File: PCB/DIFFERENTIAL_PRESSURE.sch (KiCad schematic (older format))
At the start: 6 parts

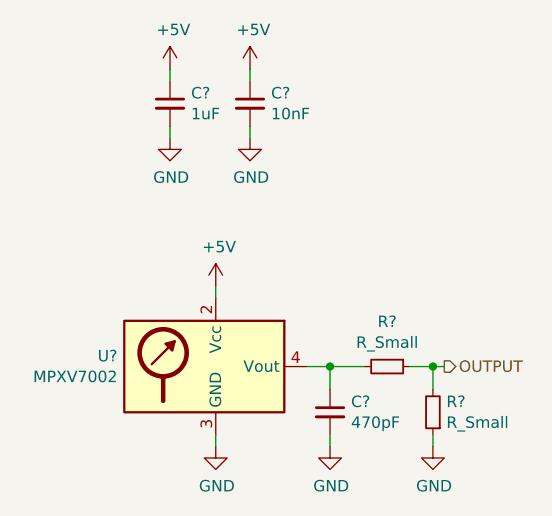
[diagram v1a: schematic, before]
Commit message: Connected Differential pressure sensor
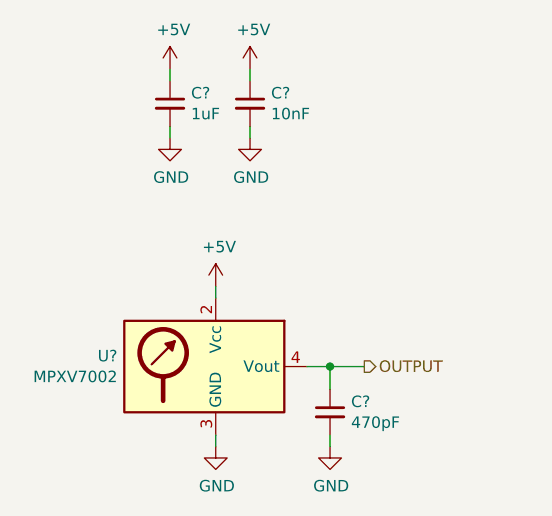
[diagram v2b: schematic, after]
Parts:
- removed R? (x2): R_Small, symbol Device:R_Small
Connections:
- net OUTPUT: now also C?.1, U?.4 (Vout)
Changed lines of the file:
@@
 Wire Wire Line
 	6550 4150 6550 4200
-$Comp
-L Device:R_Small R?
-U 1 1 5E8DE8A9
-P 6800 3850
-F 0 "R?" V 6604 3850 50  0000 C CNN
-F 1 "R_Small" V 6695 3850 50  0000 C CNN
-F 2 "" H 6800 3850 50  0001 C CNN
-F 3 "~" H 6800 3850 50  0001 C CNN
-	1    6800 3850
-	0    1    1    0
-$EndComp
-$Comp
-L Device:R_Small R?
-U 1 1 5E8DED03
-P 7000 4050
-F 0 "R?" H 6941 4004 50  0000 R CNN
-F 1 "R_Small" H 6941 4095 50  0000 R CNN
-F 2 "" H 7000 4050 50  0001 C CNN
-F 3 "~" H 7000 4050 50  0001 C CNN
-	1    7000 4050
-	-1   0    0    1
-$EndComp
 Wire Wire Line
 	6700 3850 6550 3850
 Connection ~ 6550 3850
-Wire Wire Line
-	6900 3850 7000 3850
-Wire Wire Line
-	7000 3850 7000 3950
-$Comp
-L power:GND #PWR?
-U 1 1 5E8DF45E
-P 7000 4200
-F 0 "#PWR?" H 7000 3950 50  0001 C CNN
-F 1 "GND" H 7005 4027 50  0000 C CNN
-F 2 "" H 7000 4200 50  0001 C CNN
-F 3 "" H 7000 4200 50  0001 C CNN
-	1    7000 4200
-	1    0    0    -1
-$EndComp
-Wire Wire Line
-	7000 4150 7000 4200
-Text HLabel 7050 3850 2    50   Output ~ 0
+Text HLabel 6700 3850 2    50   Output ~ 0
 OUTPUT
-Wire Wire Line
-	7050 3850 7000 3850
-Connection ~ 7000 3850
 $EndSCHEMATC

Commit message: Added Humidity and temperature sensors
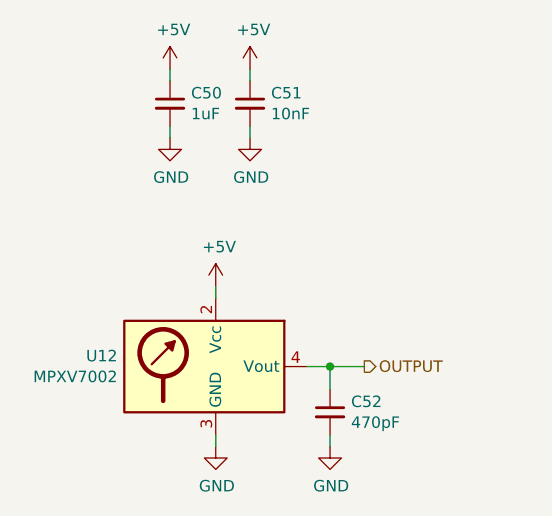
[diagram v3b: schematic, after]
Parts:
- C50, C51, C52: renamed from C?; Dielectric (none) -> X7R; Voltage Rating (none) -> 6.3V
- gave numbers to parts that had none: 1
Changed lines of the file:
@@
 $EndDescr
 $Comp
-L Sensor_Pressure:MPXA6115A U?
+L Sensor_Pressure:MPXA6115A U12
 U 1 1 5E8D808E
 P 6050 3850
-F 0 "U?" H 5620 3896 50  0000 R CNN
+F 0 "U12" H 5620 3896 50  0000 R CNN
 F 1 "MPXV7002" H 5620 3805 50  0000 R CNN
 F 2 "" H 5550 3500 50  0001 C CNN
@@
 $EndComp
 $Comp
-L power:+5V #PWR?
+L power:+5V #PWR0163
 U 1 1 5E8D8C73
 P 6050 3500
-F 0 "#PWR?" H 6050 3350 50  0001 C CNN
+F 0 "#PWR0163" H 6050 3350 50  0001 C CNN
 F 1 "+5V" H 6065 3673 50  0000 C CNN
 F 2 "" H 6050 3500 50  0001 C CNN
@@
 	6050 3500 6050 3550
 $Comp
-L power:GND #PWR?
+L power:GND #PWR0164
 U 1 1 5E8D8EEF
 P 6050 4200
-F 0 "#PWR?" H 6050 3950 50  0001 C CNN
+F 0 "#PWR0164" H 6050 3950 50  0001 C CNN
 F 1 "GND" H 6055 4027 50  0000 C CNN
 F 2 "" H 6050 4200 50  0001 C CNN
@@
 	6050 4150 6050 4200
 $Comp
-L Device:C_Small C?
+L Device:C_Small C50
 U 1 1 5E8D99D2
 P 5850 2700
-F 0 "C?" H 5942 2746 50  0000 L CNN
+F 0 "C50" H 5942 2746 50  0000 L CNN
 F 1 "1uF" H 5942 2655 50  0000 L CNN
 F 2 "" H 5850 2700 50  0001 C CNN
 F 3 "~" H 5850 2700 50  0001 C CNN
+F 4 "X7R" H 5850 2700 50  0001 C CNN "Dielectric"
+F 5 "6.3V" H 5850 2700 50  0001 C CNN "Voltage Rating"
 	1    5850 2700
 	1    0    0    -1
 $EndComp
 $Comp
-L Device:C_Small C?
+L Device:C_Small C51
 U 1 1 5E8D9CEE
 P 6200 2700
-F 0 "C?" H 6292 2746 50  0000 L CNN
+F 0 "C51" H 6292 2746 50  0000 L CNN
 F 1 "10nF" H 6292 2655 50  0000 L CNN
 F 2 "" H 6200 2700 50  0001 C CNN
 F 3 "~" H 6200 2700 50  0001 C CNN
+F 4 "X7R" H 6200 2700 50  0001 C CNN "Dielectric"
+F 5 "6.3V" H 6200 2700 50  0001 C CNN "Voltage Rating"
 	1    6200 2700
 	1    0    0    -1
 $EndComp
 $Comp
-L power:+5V #PWR?
+L power:+5V #PWR0161
 U 1 1 5E8DA334
 P 5850 2550
-F 0 "#PWR?" H 5850 2400 50  0001 C CNN
+F 0 "#PWR0161" H 5850 2400 50  0001 C CNN
 F 1 "+5V" H 5865 2723 50  0000 C CNN
 F 2 "" H 5850 2550 50  0001 C CNN
@@
 $EndComp
 $Comp
-L power:+5V #PWR?
+L power:+5V #PWR0165
 U 1 1 5E8DA611
 P 6200 2550
-F 0 "#PWR?" H 6200 2400 50  0001 C CNN
+F 0 "#PWR0165" H 6200 2400 50  0001 C CNN
 F 1 "+5V" H 6215 2723 50  0000 C CNN
 F 2 "" H 6200 2550 50  0001 C CNN
@@
 $EndComp
 $Comp
-L power:GND #PWR?
+L power:GND #PWR0162
 U 1 1 5E8DAFA6
 P 5850 2850
-F 0 "#PWR?" H 5850 2600 50  0001 C CNN
+F 0 "#PWR0162" H 5850 2600 50  0001 C CNN
 F 1 "GND" H 5855 2677 50  0000 C CNN
 F 2 "" H 5850 2850 50  0001 C CNN
@@
 $EndComp
 $Comp
-L power:GND #PWR?
+L power:GND #PWR0166
 U 1 1 5E8DB19D
 P 6200 2850
-F 0 "#PWR?" H 6200 2600 50  0001 C CNN
+F 0 "#PWR0166" H 6200 2600 50  0001 C CNN
 F 1 "GND" H 6205 2677 50  0000 C CNN
 F 2 "" H 6200 2850 50  0001 C CNN
@@
 	6200 2800 6200 2850
 $Comp
-L Device:C_Small C?
+L Device:C_Small C52
 U 1 1 5E8DD64D
 P 6550 4050
-F 0 "C?" H 6642 4096 50  0000 L CNN
+F 0 "C52" H 6642 4096 50  0000 L CNN
 F 1 "470pF" H 6642 4005 50  0000 L CNN
 F 2 "" H 6550 4050 50  0001 C CNN
 F 3 "~" H 6550 4050 50  0001 C CNN
+F 4 "X7R" H 6550 4050 50  0001 C CNN "Dielectric"
+F 5 "6.3V" H 6550 4050 50  0001 C CNN "Voltage Rating"
 	1    6550 4050
 	1    0    0    -1
@@
 	6550 3850 6550 3950
 $Comp
-L power:GND #PWR?
+L power:GND #PWR0167
 U 1 1 5E8DDD59
 P 6550 4200
-F 0 "#PWR?" H 6550 3950 50  0001 C CNN
+F 0 "#PWR0167" H 6550 3950 50  0001 C CNN
 F 1 "GND" H 6555 4027 50  0000 C CNN
 F 2 "" H 6550 4200 50  0001 C CNN

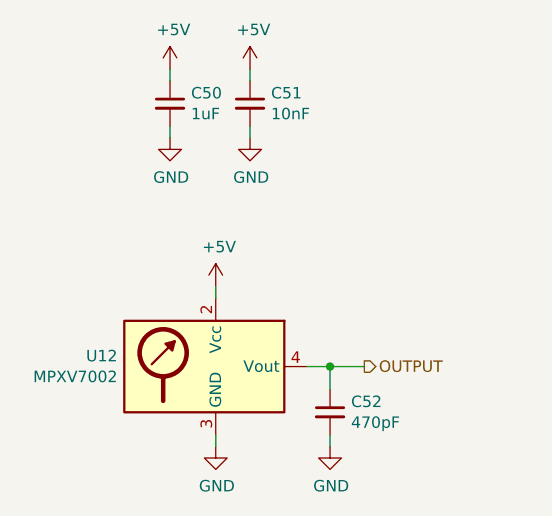
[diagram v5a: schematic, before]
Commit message: Added test points to sensors
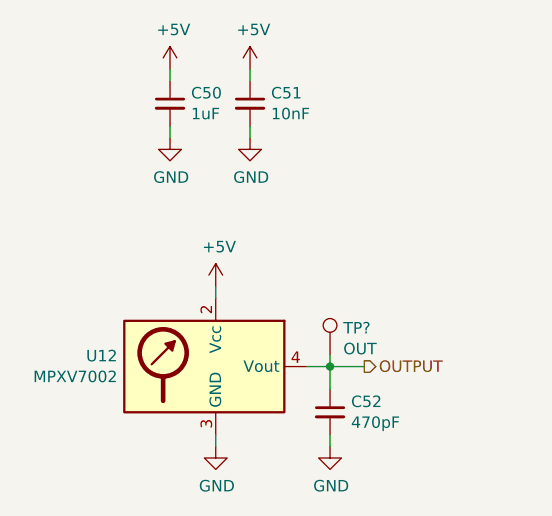
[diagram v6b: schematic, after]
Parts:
- added TP?: OUT, symbol Connector:TestPoint
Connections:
- net OUTPUT: now also TP?.1
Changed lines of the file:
@@
 $Descr A4 11693 8268
 encoding utf-8
-Sheet 25 22
+Sheet 22 22
 Title ""
 Date ""
@@
 Text HLabel 6700 3850 2    50   Output ~ 0
 OUTPUT
+$Comp
+L Connector:TestPoint TP?
+U 1 1 5E93676E
+P 6550 3800
+AR Path="/5E93676E" Ref="TP?"  Part="1"
+AR Path="/5E8D7701/5E93676E" Ref="TP?"  Part="1"
+F 0 "TP?" H 6608 3918 50  0000 L CNN
+F 1 "OUT" H 6608 3827 50  0000 L CNN
+F 2 "" H 6750 3800 50  0001 C CNN
+F 3 "~" H 6750 3800 50  0001 C CNN
+	1    6550 3800
+	1    0    0    -1
+$EndComp
+Wire Wire Line
+	6550 3800 6550 3850
 $EndSCHEMATC

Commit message: Added correct DRV breakout and added testpoints
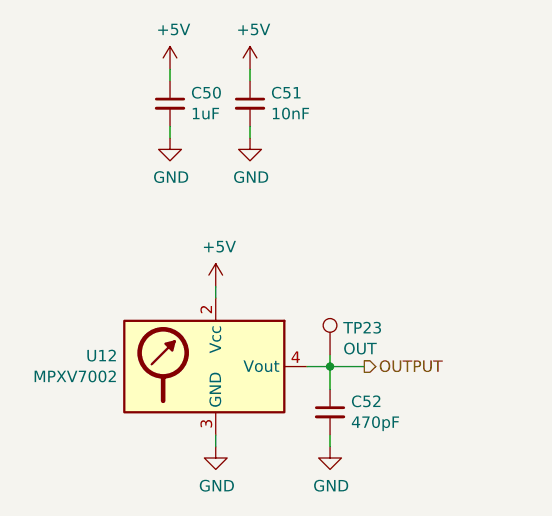
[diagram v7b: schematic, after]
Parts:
- gave numbers to parts that had none: 1
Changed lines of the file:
@@
 P 6550 3800
 AR Path="/5E93676E" Ref="TP?"  Part="1"
-AR Path="/5E8D7701/5E93676E" Ref="TP?"  Part="1"
-F 0 "TP?" H 6608 3918 50  0000 L CNN
+AR Path="/5E8D7701/5E93676E" Ref="TP23"  Part="1"
+F 0 "TP23" H 6608 3918 50  0000 L CNN
 F 1 "OUT" H 6608 3827 50  0000 L CNN
 F 2 "" H 6750 3800 50  0001 C CNN

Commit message: Added remaining test points
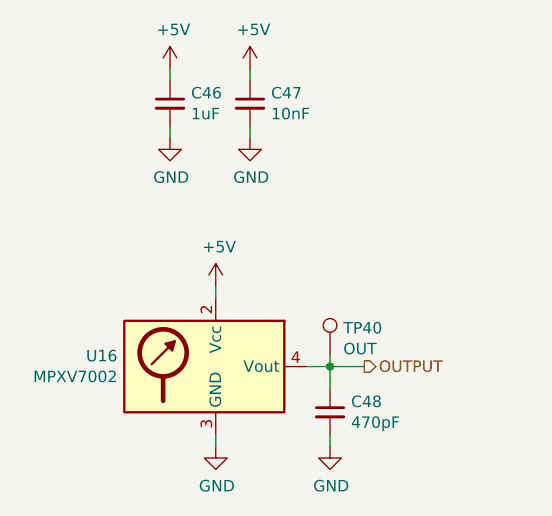
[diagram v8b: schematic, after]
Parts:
- renumbered C50 to C46, C51 to C47, C52 to C48, TP23 to TP40, U12 to U16
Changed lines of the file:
@@
 $EndDescr
 $Comp
-L Sensor_Pressure:MPXA6115A U12
+L Sensor_Pressure:MPXA6115A U16
 U 1 1 5E8D808E
 P 6050 3850
-F 0 "U12" H 5620 3896 50  0000 R CNN
+F 0 "U16" H 5620 3896 50  0000 R CNN
 F 1 "MPXV7002" H 5620 3805 50  0000 R CNN
 F 2 "" H 5550 3500 50  0001 C CNN
@@
 $EndComp
 $Comp
-L power:+5V #PWR0163
+L power:+5V #PWR0149
 U 1 1 5E8D8C73
 P 6050 3500
-F 0 "#PWR0163" H 6050 3350 50  0001 C CNN
+F 0 "#PWR0149" H 6050 3350 50  0001 C CNN
 F 1 "+5V" H 6065 3673 50  0000 C CNN
 F 2 "" H 6050 3500 50  0001 C CNN
@@
 	6050 3500 6050 3550
 $Comp
-L power:GND #PWR0164
+L power:GND #PWR0150
 U 1 1 5E8D8EEF
 P 6050 4200
-F 0 "#PWR0164" H 6050 3950 50  0001 C CNN
+F 0 "#PWR0150" H 6050 3950 50  0001 C CNN
 F 1 "GND" H 6055 4027 50  0000 C CNN
 F 2 "" H 6050 4200 50  0001 C CNN
@@
 	6050 4150 6050 4200
 $Comp
-L Device:C_Small C50
+L Device:C_Small C46
 U 1 1 5E8D99D2
 P 5850 2700
-F 0 "C50" H 5942 2746 50  0000 L CNN
+F 0 "C46" H 5942 2746 50  0000 L CNN
 F 1 "1uF" H 5942 2655 50  0000 L CNN
 F 2 "" H 5850 2700 50  0001 C CNN
@@
 $EndComp
 $Comp
-L Device:C_Small C51
+L Device:C_Small C47
 U 1 1 5E8D9CEE
 P 6200 2700
-F 0 "C51" H 6292 2746 50  0000 L CNN
+F 0 "C47" H 6292 2746 50  0000 L CNN
 F 1 "10nF" H 6292 2655 50  0000 L CNN
 F 2 "" H 6200 2700 50  0001 C CNN
@@
 $EndComp
 $Comp
-L power:+5V #PWR0161
+L power:+5V #PWR0147
 U 1 1 5E8DA334
 P 5850 2550
-F 0 "#PWR0161" H 5850 2400 50  0001 C CNN
+F 0 "#PWR0147" H 5850 2400 50  0001 C CNN
 F 1 "+5V" H 5865 2723 50  0000 C CNN
 F 2 "" H 5850 2550 50  0001 C CNN
@@
 $EndComp
 $Comp
-L power:+5V #PWR0165
+L power:+5V #PWR0151
 U 1 1 5E8DA611
 P 6200 2550
-F 0 "#PWR0165" H 6200 2400 50  0001 C CNN
+F 0 "#PWR0151" H 6200 2400 50  0001 C CNN
 F 1 "+5V" H 6215 2723 50  0000 C CNN
 F 2 "" H 6200 2550 50  0001 C CNN
@@
 $EndComp
 $Comp
-L power:GND #PWR0162
+L power:GND #PWR0148
 U 1 1 5E8DAFA6
 P 5850 2850
-F 0 "#PWR0162" H 5850 2600 50  0001 C CNN
+F 0 "#PWR0148" H 5850 2600 50  0001 C CNN
 F 1 "GND" H 5855 2677 50  0000 C CNN
 F 2 "" H 5850 2850 50  0001 C CNN
@@
 $EndComp
 $Comp
-L power:GND #PWR0166
+L power:GND #PWR0152
 U 1 1 5E8DB19D
 P 6200 2850
-F 0 "#PWR0166" H 6200 2600 50  0001 C CNN
+F 0 "#PWR0152" H 6200 2600 50  0001 C CNN
 F 1 "GND" H 6205 2677 50  0000 C CNN
 F 2 "" H 6200 2850 50  0001 C CNN
@@
 	6200 2800 6200 2850
 $Comp
-L Device:C_Small C52
+L Device:C_Small C48
 U 1 1 5E8DD64D
 P 6550 4050
-F 0 "C52" H 6642 4096 50  0000 L CNN
+F 0 "C48" H 6642 4096 50  0000 L CNN
 F 1 "470pF" H 6642 4005 50  0000 L CNN
 F 2 "" H 6550 4050 50  0001 C CNN
@@
 	6550 3850 6550 3950
 $Comp
-L power:GND #PWR0167
+L power:GND #PWR0153
 U 1 1 5E8DDD59
 P 6550 4200
-F 0 "#PWR0167" H 6550 3950 50  0001 C CNN
+F 0 "#PWR0153" H 6550 3950 50  0001 C CNN
 F 1 "GND" H 6555 4027 50  0000 C CNN
 F 2 "" H 6550 4200 50  0001 C CNN
@@
 P 6550 3800
 AR Path="/5E93676E" Ref="TP?"  Part="1"
-AR Path="/5E8D7701/5E93676E" Ref="TP23"  Part="1"
-F 0 "TP23" H 6608 3918 50  0000 L CNN
+AR Path="/5E8D7701/5E93676E" Ref="TP40"  Part="1"
+F 0 "TP40" H 6608 3918 50  0000 L CNN
 F 1 "OUT" H 6608 3827 50  0000 L CNN
 F 2 "" H 6750 3800 50  0001 C CNN
